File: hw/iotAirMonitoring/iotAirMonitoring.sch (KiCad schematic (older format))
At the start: 60 parts, among them J15 SMA, J4 PROGRAMMER, J6 EN_3V3_PROGRAMMER, Q1 MMBT3904, Q14 AO3401A, Q15 2N7002, Q2 MMBT3904, SW1 PWR_ON, SW2 PWR_OFF, SW3 RESET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

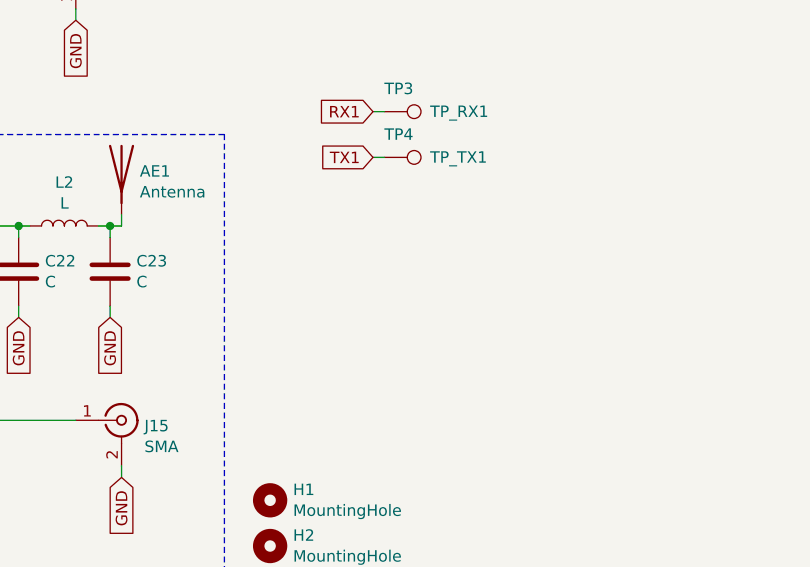
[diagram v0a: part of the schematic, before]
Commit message: Add TestPads, improve silkscreen
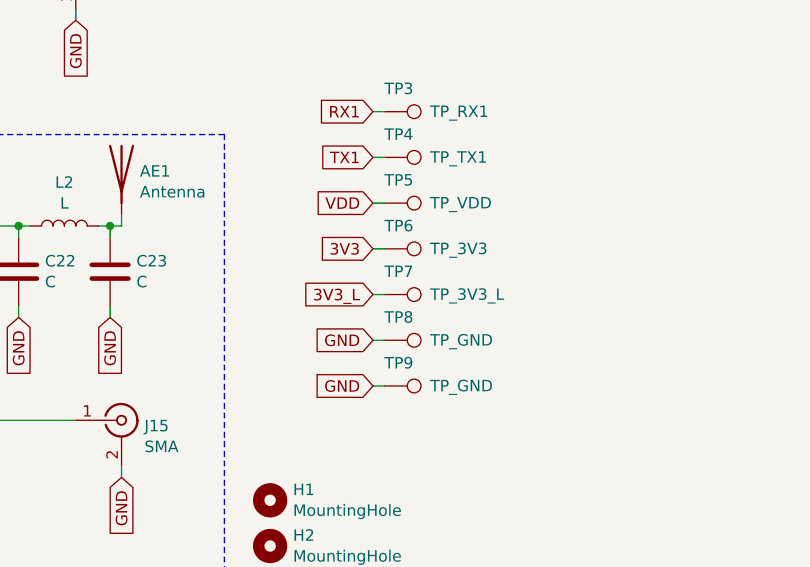
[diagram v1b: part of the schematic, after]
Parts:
- added TP5: TP_VDD, TestPoint:TestPoint_Pad_D1.5mm, symbol Connector:TestPoint
- added TP6: TP_3V3, TestPoint:TestPoint_Pad_D1.5mm, symbol Connector:TestPoint
- added TP7: TP_3V3_L, TestPoint:TestPoint_Pad_D1.5mm, symbol Connector:TestPoint
- added TP8, TP9: TP_GND, TestPoint:TestPoint_Pad_D1.5mm, symbol Connector:TestPoint
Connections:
- net 3V3: now also TP6.1
- net 3V3_L: now also TP7.1
- net GND: now also TP8.1, TP9.1
- net VDD: now also TP5.1
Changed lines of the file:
@@
 Wire Wire Line
 	4650 6500 5100 6500
+$Comp
+L Connector:TestPoint TP5
+U 1 1 6182AB5D
+P 6450 5550
+F 0 "TP5" V 6350 5550 50  0000 L CNN
+F 1 "TP_VDD" V 6450 5750 50  0000 L CNN
+F 2 "TestPoint:TestPoint_Pad_D1.5mm" H 6650 5550 50  0001 C CNN
+F 3 "~" H 6650 5550 50  0001 C CNN
+	1    6450 5550
+	0    1    1    0
+$EndComp
+$Comp
+L Connector:TestPoint TP6
+U 1 1 6182B01D
+P 6450 5750
+F 0 "TP6" V 6350 5750 50  0000 L CNN
+F 1 "TP_3V3" V 6450 5950 50  0000 L CNN
+F 2 "TestPoint:TestPoint_Pad_D1.5mm" H 6650 5750 50  0001 C CNN
+F 3 "~" H 6650 5750 50  0001 C CNN
+	1    6450 5750
+	0    1    1    0
+$EndComp
+$Comp
+L Connector:TestPoint TP7
+U 1 1 6182B3F1
+P 6450 5950
+F 0 "TP7" V 6350 5950 50  0000 L CNN
+F 1 "TP_3V3_L" V 6450 6150 50  0000 L CNN
+F 2 "TestPoint:TestPoint_Pad_D1.5mm" H 6650 5950 50  0001 C CNN
+F 3 "~" H 6650 5950 50  0001 C CNN
+	1    6450 5950
+	0    1    1    0
+$EndComp
+Text GLabel 6400 5550 0    50   Input ~ 0
+VDD
+Text GLabel 6400 5750 0    50   Input ~ 0
+3V3
+Text GLabel 6400 5950 0    50   Input ~ 0
+3V3_L
+Wire Wire Line
+	6400 5950 6450 5950
+Wire Wire Line
+	6450 5750 6400 5750
+Wire Wire Line
+	6400 5550 6450 5550
+$Comp
+L Connector:TestPoint TP8
+U 1 1 6185F485
+P 6450 6150
+F 0 "TP8" V 6350 6150 50  0000 L CNN
+F 1 "TP_GND" V 6450 6350 50  0000 L CNN
+F 2 "TestPoint:TestPoint_Pad_D1.5mm" H 6650 6150 50  0001 C CNN
+F 3 "~" H 6650 6150 50  0001 C CNN
+	1    6450 6150
+	0    1    1    0
+$EndComp
+$Comp
+L Connector:TestPoint TP9
+U 1 1 6185F92C
+P 6450 6350
+F 0 "TP9" V 6350 6350 50  0000 L CNN
+F 1 "TP_GND" V 6450 6550 50  0000 L CNN
+F 2 "TestPoint:TestPoint_Pad_D1.5mm" H 6650 6350 50  0001 C CNN
+F 3 "~" H 6650 6350 50  0001 C CNN
+	1    6450 6350
+	0    1    1    0
+$EndComp
+Wire Wire Line
+	6450 6150 6400 6150
+Wire Wire Line
+	6400 6350 6450 6350
+Text GLabel 6400 6150 0    50   Input ~ 0
+GND
+Text GLabel 6400 6350 0    50   Input ~ 0
+GND
 $EndSCHEMATC

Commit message: Create Makefile for gerbers generation, type in missing LCSC codes
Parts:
- Q15: LCSC (none) -> C8545
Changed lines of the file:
@@
 F 2 "Package_TO_SOT_SMD:SOT-23" H 2000 6575 50  0001 L CIN
 F 3 "https://www.onsemi.com/pub/Collateral/NDS7002A-D.PDF" H 1800 6650 50  0001 L CNN
+F 4 "C8545" V 1800 6650 50  0001 C CNN "LCSC"
 	1    1800 6650
 	-1   0    0    -1

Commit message: Add JLCPCB assembly correction, generate gerber data
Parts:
- Q1, Q14, Q15, Q2: JLCPCB_CORRECTIONS (none) -> 0;0;180
- U1: JLCPCB_CORRECTIONS (none) -> 0;0;270
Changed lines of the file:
@@
 F 3 "https://www.espressif.com/sites/default/files/documentation/esp32-wroom-32_datasheet_en.pdf" H 4800 3350 50  0001 C CNN
 F 4 "C82899" H 5100 3300 50  0001 C CNN "LCSC"
+F 5 "0;0;270" H 5100 3300 50  0001 C CNN "JLCPCB_CORRECTIONS"
 	1    5100 3300
 	1    0    0    -1
@@
 F 3 "~" H 2300 4050 50  0001 C CNN
 F 4 "C20526" H 2300 4050 50  0001 C CNN "LCSC"
+F 5 "0;0;180" H 2300 4050 50  0001 C CNN "JLCPCB_CORRECTIONS"
 	1    2300 4050
 	1    0    0    -1
@@
 F 3 "~" H 1750 4500 50  0001 C CNN
 F 4 "C20526" H 1750 4500 50  0001 C CNN "LCSC"
+F 5 "0;0;180" H 1750 4500 50  0001 C CNN "JLCPCB_CORRECTIONS"
 	1    1750 4500
 	1    0    0    1
@@
 F 3 "https://www.onsemi.com/pub/Collateral/NDS7002A-D.PDF" H 1800 6650 50  0001 L CNN
 F 4 "C8545" V 1800 6650 50  0001 C CNN "LCSC"
+F 5 "0;0;180" V 1800 6650 50  0001 C CNN "JLCPCB_CORRECTIONS"
 	1    1800 6650
 	-1   0    0    -1
@@
 F 3 "https://datasheet.lcsc.com/lcsc/1810171817_Alpha-&-Omega-Semicon-AO3401A_C15127.pdf" H 1700 6100 50  0001 C CNN
 F 4 "C15127" V 1700 6100 50  0001 C CNN "LCSC"
+F 5 "0;0;180" V 1700 6100 50  0001 C CNN "JLCPCB_CORRECTIONS"
 	1    1700 6100
 	0    1    -1   0
